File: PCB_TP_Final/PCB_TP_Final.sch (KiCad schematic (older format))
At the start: 4 parts, among them CN10 Conn_02x17_Odd_Even, CN7 Conn_02x10_Odd_Even, CN8 Conn_02x08_Odd_Even, CN9 Conn_02x15_Odd_Even

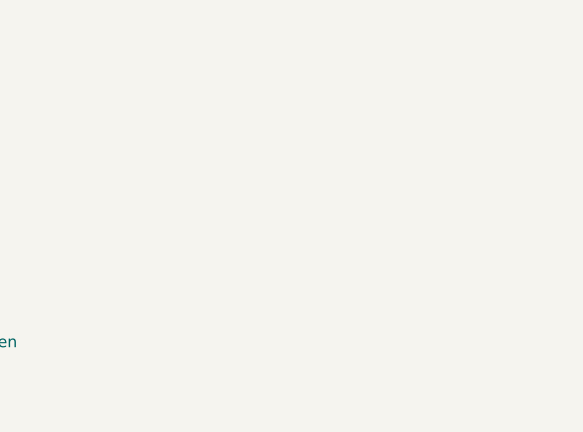
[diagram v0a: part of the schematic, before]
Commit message: Add 3D conections and NODEMCU ESP12
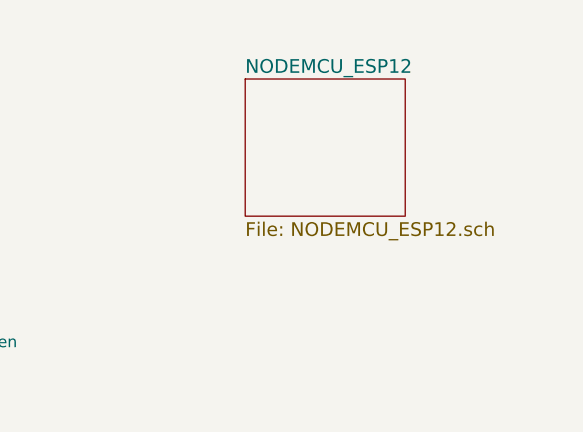
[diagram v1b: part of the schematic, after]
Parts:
- CN7: footprint Connector_PinHeader_2.54mm:PinHeader_2x10_P2.54mm_Vertical -> Pin_Headers:Pin_Header_Straight_2x07_Pitch2.54mm
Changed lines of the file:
@@
 LIBS:contrib
 LIBS:valves
+LIBS:nodemcu_esp12
 LIBS:PCB_TP_Final-cache
 EELAYER 25 0
@@
 $Descr A4 11693 8268
 encoding utf-8
-Sheet 1 2
+Sheet 1 3
 Title ""
 Date ""
@@
 F 0 "CN7" H 5300 2700 50  0000 C CNN
 F 1 "Conn_02x10_Odd_Even" H 5300 1600 50  0000 C CNN
-F 2 "Connector_PinHeader_2.54mm:PinHeader_2x10_P2.54mm_Vertical" H 5250 2200 50  0001 C CNN
+F 2 "Pin_Headers:Pin_Header_Straight_2x07_Pitch2.54mm" H 5250 2200 50  0001 C CNN
 F 3 "" H 5250 2200 50  0001 C CNN
 	1    5250 2200
@@
 Wire Wire Line
 	3750 1900 3850 1900
+$Sheet
+S 6700 1650 700  600
+U 5BA67DD8
+F0 "NODEMCU_ESP12" 60
+F1 "NODEMCU_ESP12.sch" 60
+$EndSheet
 $EndSCHEMATC

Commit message: Primera entrega (1.0) para revision
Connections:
- net GND: now also CN9.12 (Pin_12)
- net NODEMCU_ESP12/HMISO: now reaches CN10.10 (Pin_10)
- net NODEMCU_ESP12/HSCLK: now reaches CN10.26 (Pin_26)
- net NODEMCU_ESP12/HMOSI: now reaches CN10.28 (Pin_28)
- net NODEMCU_ESP12/HCS: now reaches CN10.6 (Pin_6)
- net +3V3 renamed 3.3VB
- no-connect marks 92 -> 87
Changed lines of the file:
@@
 LIBS:valves
 LIBS:nodemcu_esp12
+LIBS:power_mb_v2
 LIBS:PCB_TP_Final-cache
 EELAYER 25 0
@@
 $Descr A4 11693 8268
 encoding utf-8
-Sheet 1 3
-Title ""
-Date ""
-Rev ""
-Comp ""
+Sheet 1 4
+Title "SHIELD VoIP para NUCLEO F767"
+Date "2018-09-26"
+Rev "1.0"
+Comp "Ericson Joseph Estupiñan "
 Comment1 ""
 Comment2 ""
@@
 NoConn ~ 5550 4600
 NoConn ~ 5550 4500
-NoConn ~ 5550 4400
-NoConn ~ 5550 4300
 NoConn ~ 5550 4200
 NoConn ~ 5550 4100
@@
 NoConn ~ 5550 3700
 NoConn ~ 5550 3600
-NoConn ~ 5550 3500
 NoConn ~ 5550 3400
-NoConn ~ 5550 3300
 NoConn ~ 5550 3200
 NoConn ~ 5550 3100
@@
 NoConn ~ 3300 4000
 NoConn ~ 3300 3900
-NoConn ~ 3300 3800
 NoConn ~ 3300 3700
 NoConn ~ 3300 3600
@@
 NoConn ~ 3350 2800
 NoConn ~ 3350 2900
-$Comp
-L +3.3V #PWR02
-U 1 1 5BA5A575
-P 2450 2500
-F 0 "#PWR02" H 2450 2350 50  0001 C CNN
-F 1 "+3.3V" H 2450 2640 50  0000 C CNN
-F 2 "" H 2450 2500 50  0001 C CNN
-F 3 "" H 2450 2500 50  0001 C CNN
-	1    2450 2500
-	1    0    0    -1
-$EndComp
 NoConn ~ 3850 2000
 Wire Wire Line
@@
 	3600 1700 3850 1700
 Wire Wire Line
-	2850 2600 2450 2600
-Wire Wire Line
-	2450 2600 2450 2500
+	2450 2600 2850 2600
+Wire Wire Line
+	2450 2000 2450 2600
 Wire Wire Line
 	5550 1800 5550 1700
@@
 	3750 1900 3850 1900
 $Sheet
-S 6700 1650 700  600
+S 6600 3150 800  650
 U 5BA67DD8
 F0 "NODEMCU_ESP12" 60
 F1 "NODEMCU_ESP12.sch" 60
+F2 "HSCLK" I L 6600 3500 60
+F3 "HMISO" I L 6600 3400 60
+F4 "HMOSI" I L 6600 3600 60
+F5 "HCS" I L 6600 3300 60
 $EndSheet
+$Sheet
+S 6600 1700 800  650
+U 5BA7CCA2
+F0 "POWER_MB_V2" 60
+F1 "POWER_MB_V2.sch" 60
+$EndSheet
+Text GLabel 2300 2000 0    60   Input ~ 0
+3.3VB
+Wire Wire Line
+	2450 2000 2300 2000
+Wire Wire Line
+	5550 4300 6350 4300
+Wire Wire Line
+	6350 4300 6350 3500
+Wire Wire Line
+	6350 3500 6600 3500
+Wire Wire Line
+	5550 4400 6400 4400
+Wire Wire Line
+	6400 4400 6400 3600
+Wire Wire Line
+	6400 3600 6600 3600
+Wire Wire Line
+	5550 3500 6300 3500
+Wire Wire Line
+	6300 3500 6300 3400
+Wire Wire Line
+	6300 3400 6600 3400
+Wire Wire Line
+	5550 3300 6600 3300
+$Comp
+L GND #PWR?
+U 1 1 5BAC5062
+P 3600 3900
+F 0 "#PWR?" H 3600 3650 50  0001 C CNN
+F 1 "GND" H 3600 3750 50  0000 C CNN
+F 2 "" H 3600 3900 50  0001 C CNN
+F 3 "" H 3600 3900 50  0001 C CNN
+	1    3600 3900
+	1    0    0    -1
+$EndComp
+Wire Wire Line
+	3300 3800 3600 3800
+Wire Wire Line
+	3600 3800 3600 3900
 $EndSCHEMATC

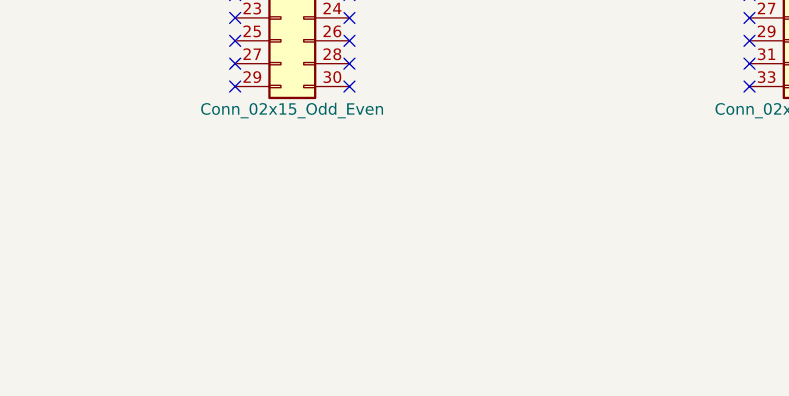
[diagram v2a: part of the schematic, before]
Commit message: Add size modify and mounting holes
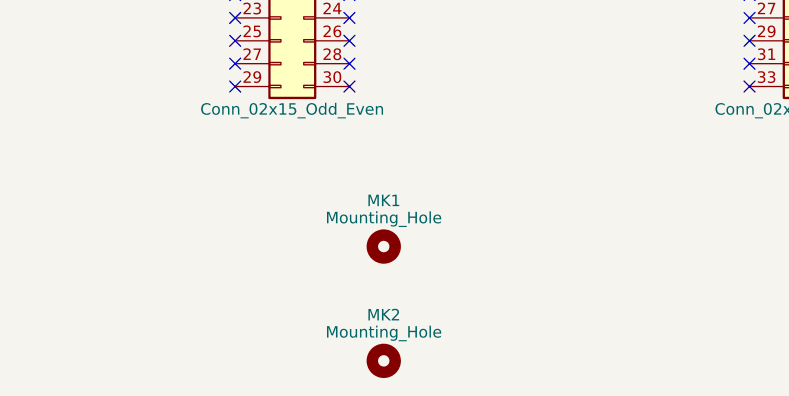
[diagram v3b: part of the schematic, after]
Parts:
- added MK1, MK2: Mounting_Hole, Mounting_Holes:MountingHole_3.7mm, symbol Mounting_Hole
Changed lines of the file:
@@
 LIBS:nodemcu_esp12
 LIBS:power_mb_v2
+LIBS:Mechanical
 LIBS:PCB_TP_Final-cache
 EELAYER 25 0
@@
 	5550 3300 6600 3300
 $Comp
-L GND #PWR?
+L GND #PWR02
 U 1 1 5BAC5062
 P 3600 3900
-F 0 "#PWR?" H 3600 3650 50  0001 C CNN
+F 0 "#PWR02" H 3600 3650 50  0001 C CNN
 F 1 "GND" H 3600 3750 50  0000 C CNN
 F 2 "" H 3600 3900 50  0001 C CNN
@@
 Wire Wire Line
 	3600 3800 3600 3900
+$Comp
+L Mounting_Hole MK1
+U 1 1 5BB85397
+P 3450 5400
+F 0 "MK1" H 3450 5600 50  0000 C CNN
+F 1 "Mounting_Hole" H 3450 5525 50  0000 C CNN
+F 2 "Mounting_Holes:MountingHole_3.7mm" H 3450 5400 50  0001 C CNN
+F 3 "" H 3450 5400 50  0001 C CNN
+	1    3450 5400
+	1    0    0    -1
+$EndComp
+$Comp
+L Mounting_Hole MK2
+U 1 1 5BB8559D
+P 3450 5900
+F 0 "MK2" H 3450 6100 50  0000 C CNN
+F 1 "Mounting_Hole" H 3450 6025 50  0000 C CNN
+F 2 "Mounting_Holes:MountingHole_3.7mm" H 3450 5900 50  0001 C CNN
+F 3 "" H 3450 5900 50  0001 C CNN
+	1    3450 5900
+	1    0    0    -1
+$EndComp
 $EndSCHEMATC

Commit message: Revisión 2.0 para evaluación
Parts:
- added F1, F2: Fiducial, Fiducials:Fiducial_1mm_Dia_2.54mm_Outer_CopperBottom, symbol Mounting_Hole
- added F3, F4: Fiducial, Fiducials:Fiducial_1mm_Dia_2.54mm_Outer_CopperTop, symbol Mounting_Hole
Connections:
- net TalkButton/talk: now reaches CN9.30 (Pin_30)
- no-connect marks 87 -> 86
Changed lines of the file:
@@
 $Descr A4 11693 8268
 encoding utf-8
-Sheet 1 4
+Sheet 1 5
 Title "SHIELD VoIP para NUCLEO F767"
 Date "2018-09-26"
-Rev "1.0"
+Rev "2.0"
 Comp "Ericson Joseph Estupiñan "
 Comment1 ""
@@
 NoConn ~ 2800 4600
 NoConn ~ 2800 4700
-NoConn ~ 3300 4700
 NoConn ~ 3300 4600
 NoConn ~ 3300 4500
@@
 F0 "AUDIO_CODEC" 60
 F1 "AUDIO_CODEC.sch" 60
-F2 "SCK" I L 3850 1600 60
-F3 "MISO" I L 3850 1700 60
-F4 "MOSI" I L 3850 1800 60
-F5 "ADCL" I L 3850 1900 60
-F6 "DACL" I L 3850 2000 60
-F7 "SDA" I R 4500 1600 60
-F8 "SCL" I R 4500 1700 60
+F2 "SCK" O L 3850 1600 60
+F3 "SDA" B R 4500 1600 60
+F4 "MISO" I L 3850 1700 60
+F5 "ADCL" O L 3850 1900 60
+F6 "DACL" O L 3850 2000 60
+F7 "MOSI" O L 3850 1800 60
+F8 "SCL" O R 4500 1700 60
 $EndSheet
 NoConn ~ 3350 2800
@@
 	1    0    0    -1
 $EndComp
+$Sheet
+S 1250 4050 750  700
+U 5BBD73D1
+F0 "TalkButton" 60
+F1 "talkbutton.sch" 60
+F2 "talk" O R 2000 4600 60
+$EndSheet
+Wire Wire Line
+	3300 4700 3600 4700
+Wire Wire Line
+	3600 4700 3600 4850
+Wire Wire Line
+	3600 4850 2300 4850
+Wire Wire Line
+	2300 4850 2300 4600
+Wire Wire Line
+	2300 4600 2000 4600
+$Comp
+L Mounting_Hole F1
+U 1 1 5BC13BBA
+P 4500 5400
+F 0 "F1" H 4500 5600 50  0000 C CNN
+F 1 "Fiducial" H 4500 5525 50  0000 C CNN
+F 2 "Fiducials:Fiducial_1mm_Dia_2.54mm_Outer_CopperBottom" H 4500 5400 50  0001 C CNN
+F 3 "" H 4500 5400 50  0001 C CNN
+	1    4500 5400
+	1    0    0    -1
+$EndComp
+$Comp
+L Mounting_Hole F3
+U 1 1 5BC13CC4
+P 4500 5900
+F 0 "F3" H 4500 6100 50  0000 C CNN
+F 1 "Fiducial" H 4500 6025 50  0000 C CNN
+F 2 "Fiducials:Fiducial_1mm_Dia_2.54mm_Outer_CopperTop" H 4500 5900 50  0001 C CNN
+F 3 "" H 4500 5900 50  0001 C CNN
+	1    4500 5900
+	1    0    0    -1
+$EndComp
+$Comp
+L Mounting_Hole F2
+U 1 1 5BC13DBE
+P 5200 5400
+F 0 "F2" H 5200 5600 50  0000 C CNN
+F 1 "Fiducial" H 5200 5525 50  0000 C CNN
+F 2 "Fiducials:Fiducial_1mm_Dia_2.54mm_Outer_CopperBottom" H 5200 5400 50  0001 C CNN
+F 3 "" H 5200 5400 50  0001 C CNN
+	1    5200 5400
+	1    0    0    -1
+$EndComp
+$Comp
+L Mounting_Hole F4
+U 1 1 5BC13E5D
+P 5200 5900
+F 0 "F4" H 5200 6100 50  0000 C CNN
+F 1 "Fiducial" H 5200 6025 50  0000 C CNN
+F 2 "Fiducials:Fiducial_1mm_Dia_2.54mm_Outer_CopperTop" H 5200 5900 50  0001 C CNN
+F 3 "" H 5200 5900 50  0001 C CNN
+	1    5200 5900
+	1    0    0    -1
+$EndComp

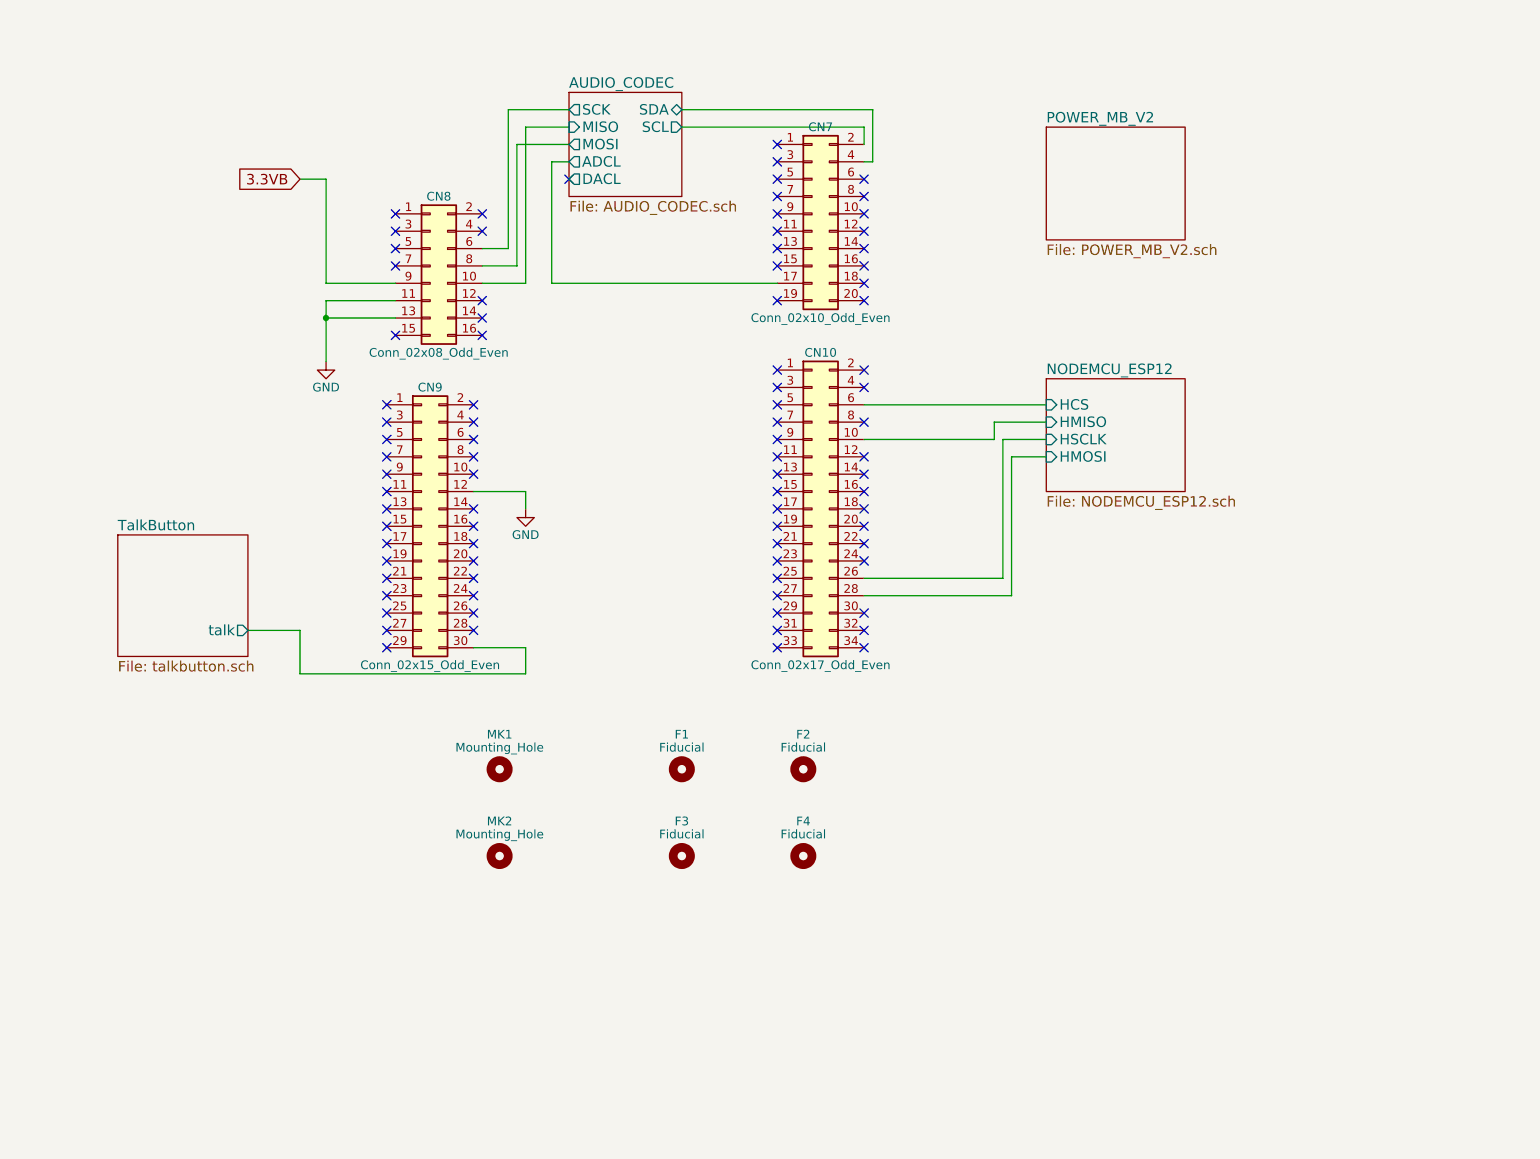
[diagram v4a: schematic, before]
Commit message: Se agregaron correcciones sugeridas
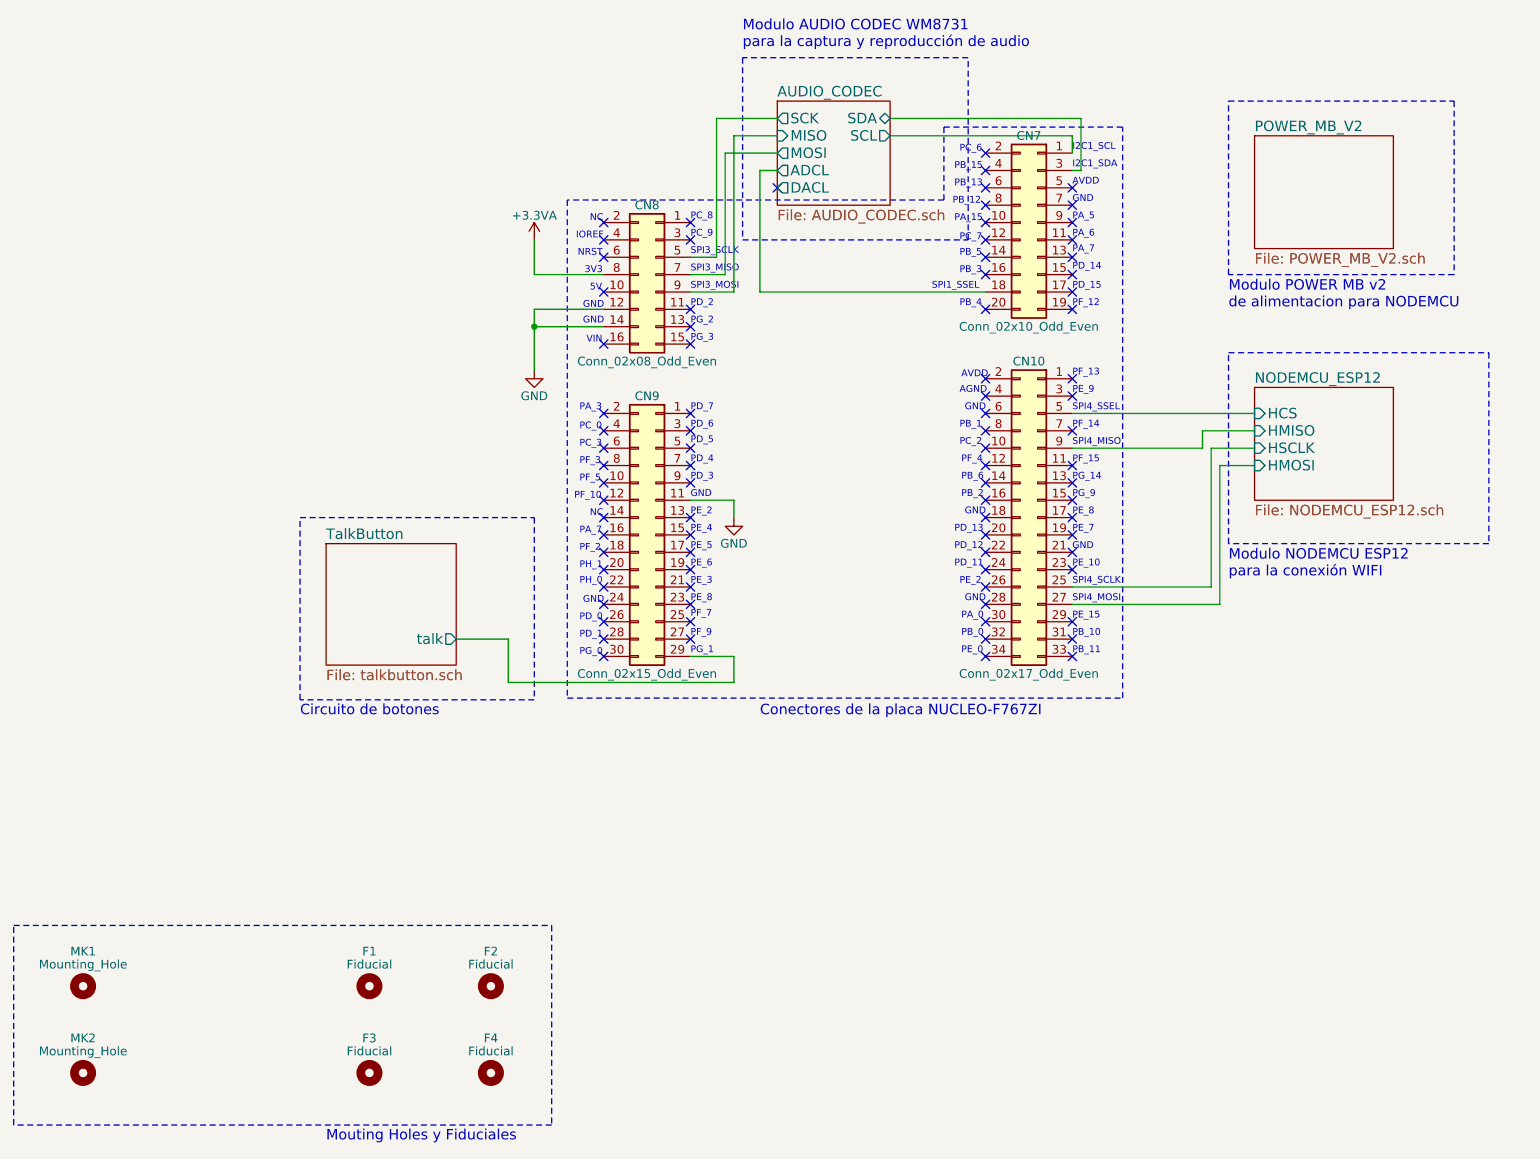
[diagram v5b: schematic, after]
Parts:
- CN10: footprint Connector_PinHeader_2.54mm:PinHeader_2x17_P2.54mm_Vertical -> Pin_Headers:Pin_Header_Straight_2x17_Pitch2.54mm
- CN7: footprint Pin_Headers:Pin_Header_Straight_2x07_Pitch2.54mm -> Pin_Headers:Pin_Header_Straight_2x10_Pitch2.54mm
- CN8: footprint Connector_PinHeader_2.54mm:PinHeader_2x08_P2.54mm_Vertical -> Pin_Headers:Pin_Header_Straight_2x08_Pitch2.54mm
- CN9: footprint Connector_PinHeader_2.54mm:PinHeader_2x15_P2.54mm_Vertical -> Pin_Headers:Pin_Header_Straight_2x15_Pitch2.54mm
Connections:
- net 3.3VB is gone; now on net AUDIO_CODEC/MISO: CN8.9 (Pin_9)
- net AUDIO_CODEC/ADCL: now also CN7.18 (Pin_18); no longer CN7.17 (Pin_17)
- net AUDIO_CODEC/MISO: no longer CN8.10 (Pin_10)
- net AUDIO_CODEC/MOSI: now also CN8.7 (Pin_7); no longer CN8.8 (Pin_8)
- net AUDIO_CODEC/SCK: now also CN8.5 (Pin_5); no longer CN8.6 (Pin_6)
- net AUDIO_CODEC/SCL: now also CN7.1 (Pin_1); no longer CN7.2 (Pin_2)
- net AUDIO_CODEC/SDA: now also CN7.3 (Pin_3); no longer CN7.4 (Pin_4)
- net GND: now also CN8.12 (Pin_12), CN8.14 (Pin_14), CN9.11 (Pin_11); no longer CN8.11 (Pin_11), CN8.13 (Pin_13), CN9.12 (Pin_12)
- net NODEMCU_ESP12/HCS: now also CN10.5 (Pin_5); no longer CN10.6 (Pin_6)
- net NODEMCU_ESP12/HMISO: now also CN10.9 (Pin_9); no longer CN10.10 (Pin_10)
- net NODEMCU_ESP12/HMOSI: now also CN10.27 (Pin_27); no longer CN10.28 (Pin_28)
- net NODEMCU_ESP12/HSCLK: now also CN10.25 (Pin_25); no longer CN10.26 (Pin_26)
- net TalkButton/talk: now also CN9.29 (Pin_29); no longer CN9.30 (Pin_30)
- new net +3.3VA: CN8.8 (Pin_8)
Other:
- note added: "3V3\n"
- note added: "5V"
- note added: "AGND"
- note added: "AVDD"
- note added: "Circuito de botones"
- note added: "Conectores de la placa NUCLEO-F767ZI"
- note added: "GND"
- note added: "I2C1_SCL"
- note added: "I2C1_SDA"
- note added: "IOREF"
- note added: "Modulo AUDIO CODEC WM8731\npara la captura y reproducción de audio"
- note added: "Modulo NODEMCU ESP12\npara la conexión WIFI"
- note added: "Modulo POWER MB v2 \nde alimentacion para NODEMCU\n"
- note added: "Mouting Holes y Fiduciales"
- note added: "NC"
- note added: "NRST"
- note added: "PA_0"
- note added: "PA_15"
- note added: "PA_3"
- note added: "PA_5"
- note added: "PA_6"
- note added: "PA_7"
- note added: "PB_0"
- note added: "PB_1"
- note added: "PB_10"
- note added: "PB_11"
- note added: "PB_12"
- note added: "PB_13"
- note added: "PB_15"
- note added: "PB_2"
- note added: "PB_3"
- note added: "PB_4"
- note added: "PB_5"
- note added: "PB_6"
- note added: "PC_0"
- note added: "PC_2"
- note added: "PC_3"
- note added: "PC_6"
- note added: "PC_7"
- note added: "PC_8"
- note added: "PC_9"
- note added: "PD_0"
- note added: "PD_1"
- note added: "PD_11"
- note added: "PD_12"
- note added: "PD_13"
- note added: "PD_14"
- note added: "PD_15"
- note added: "PD_2"
- note added: "PD_3"
- note added: "PD_4"
- note added: "PD_5"
- note added: "PD_6"
- note added: "PD_7"
- note added: "PE_0"
- note added: "PE_10"
- note added: "PE_15"
- note added: "PE_2"
- note added: "PE_3"
- note added: "PE_4"
- note added: "PE_5"
- note added: "PE_6"
- note added: "PE_7"
- note added: "PE_8"
- note added: "PE_9"
- note added: "PF_10"
- note added: "PF_12"
- note added: "PF_13"
- note added: "PF_14"
- note added: "PF_15"
- note added: "PF_2"
- note added: "PF_3"
- note added: "PF_4"
- note added: "PF_5"
- note added: "PF_7"
- note added: "PF_9"
- note added: "PG_0"
- note added: "PG_1"
- note added: "PG_14"
- note added: "PG_2"
- note added: "PG_3"
- note added: "PG_9"
- note added: "PH_0"
- note added: "PH_1"
- note added: "SPI1_SSEL"
- note added: "SPI3_MISO"
- note added: "SPI3_MOSI"
- note added: "SPI3_SCLK"
- note added: "SPI4_MISO"
- note added: "SPI4_MOSI"
- note added: "SPI4_SCLK"
- note added: "SPI4_SSEL"
- note added: "VIN"
- moved on the sheet: CN10, CN7, CN8, CN9, F1, F2, F3, F4, MK1, MK2
